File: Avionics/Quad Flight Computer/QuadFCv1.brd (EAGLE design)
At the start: 49.5 x 49.5 mm, 130 parts, among them J2 1050270001, Q1 DMP2035U, Q2 DMP2035U, Q3 DMP2035U, SW1 PTS635VL31-VERT, U1 TM4C123GH6PZ, U10 LTC4412, U11 AP7215-33YG-13, U2 74LVC4245APW, U3 ATMEGA32U2-MU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

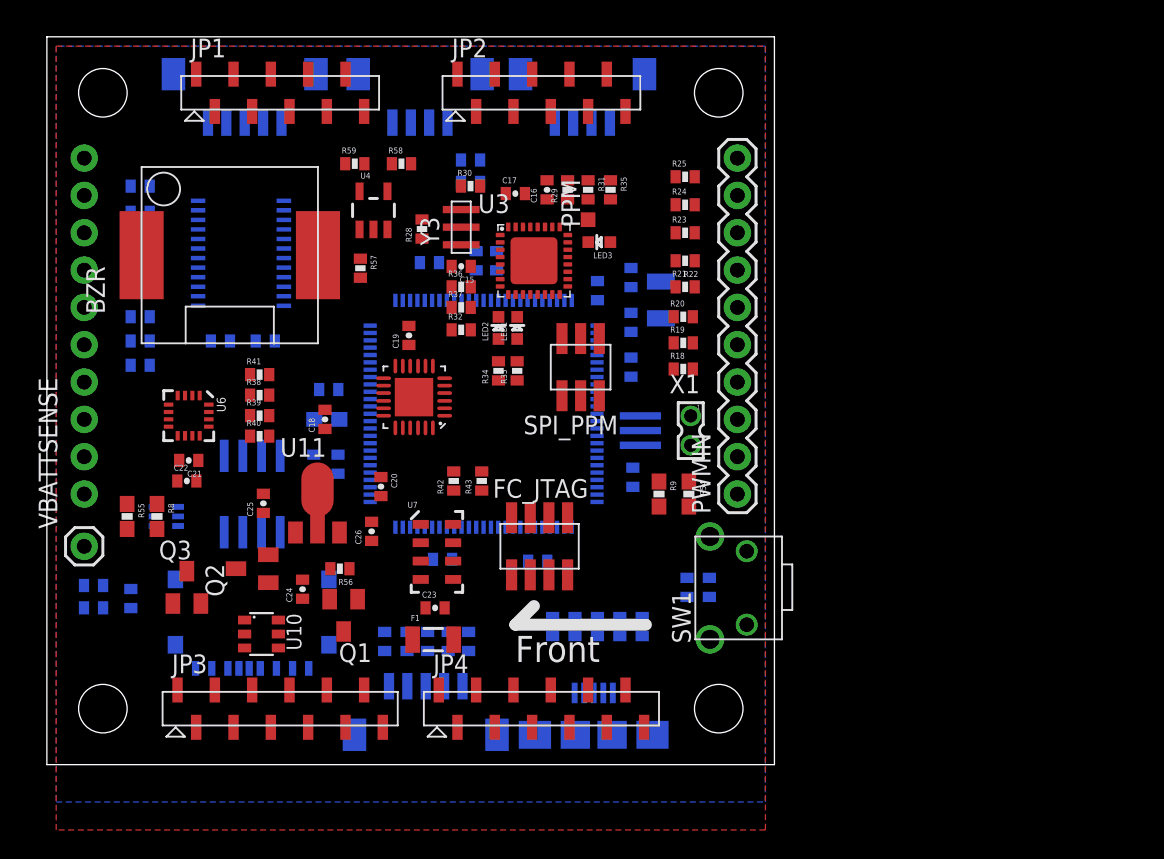
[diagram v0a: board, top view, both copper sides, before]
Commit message: Finished pinout for shield headers
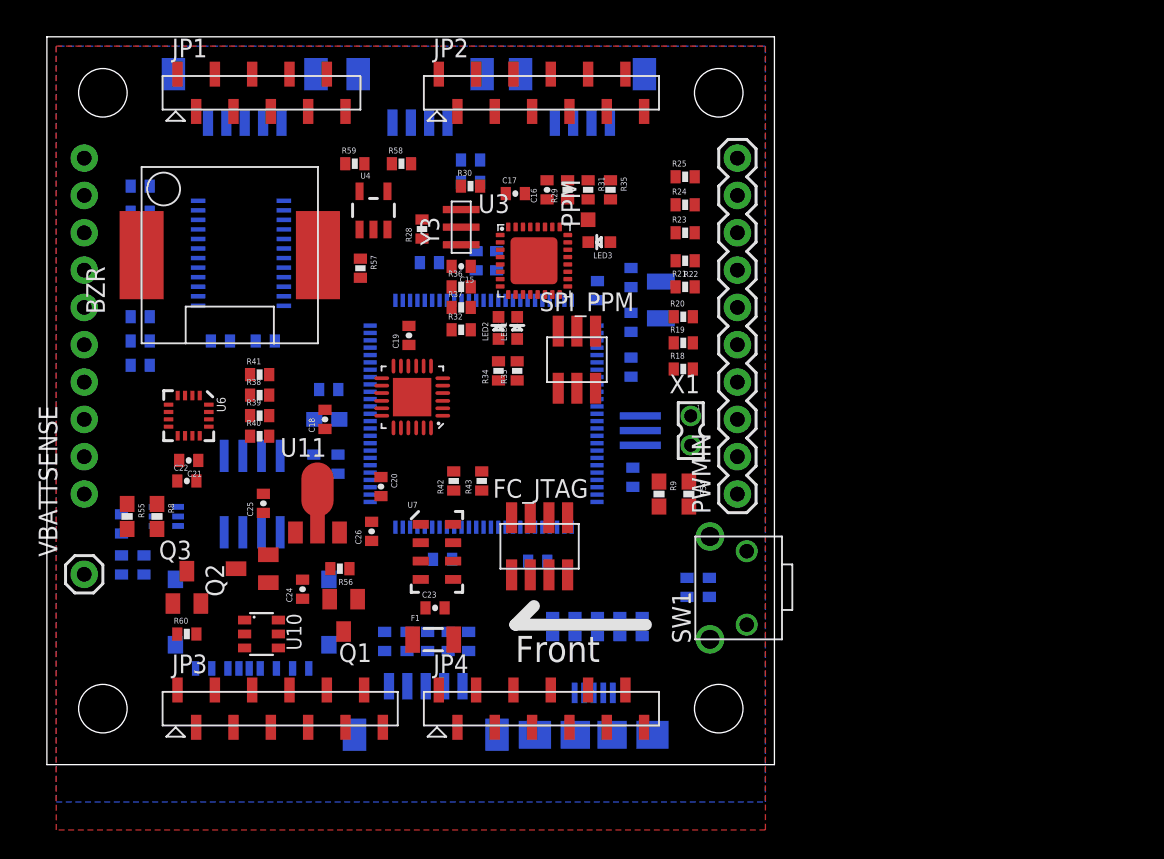
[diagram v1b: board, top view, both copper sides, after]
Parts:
- added R60: 100k, QuadFCv1:0402-RES
- JP2: value M101X10-SMT-0.05 -> M12; device QuadFCv1:1X10_SMT-0.05 -> QuadFCv1:1X12_SMT-0.05
- moved R46 5.12 mm to (5.08, 16.4)
- moved R45 4.50 mm to (6.60, 13.6), turned to 90 degrees
- moved R44 2.36 mm to (5.08, 13.6), turned to 270 degrees
- moved VBATTSENSE 1.90 mm to (2.54, 13.0)
- moved JP1 1.27 mm to (8.89, 45.7)
- moved JP2 1.27 mm to (26.7, 45.7)
- moved SPI_PPM 0.57 mm to (36.1, 27.6), turned to 0 degrees
- moved U5 0.13 mm to (24.9, 25.0)
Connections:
- net 3.3V: now also JP3.2
- net 5V: now also JP3.1
- net 5VBATT: now also R60.2
- net BUZZER_PWM: now also JP1.5
- net FC_IMU_MISO: now also JP2.2
- net FC_IMU_MOSI: now also JP2.3
- net FC_IMU_SCLK: now also JP2.1
- net FC_JTAG_TCK: now also JP4.5
- net FC_JTAG_TDI: now also JP4.7
- net FC_JTAG_TDO: now also JP4.8
- net FC_JTAG_TMS: now also JP4.6
- net FC_MEM_CLK: now also JP3.4
- net FC_MEM_MISO: now also JP3.5
- net FC_MEM_MOSI: now also JP3.3
- net FC_PB2: now also JP4.12
- net FC_PB3: now also JP4.11
- net FC_PB4: now also JP4.1
- net FC_PB5: now also JP4.2
- net FC_PD0: now also JP3.9
- net FC_PD1: now also JP3.8
- net FC_PD2: now also JP3.7
- net FC_PD3: now also JP3.6
- net FC_PD4: now also JP3.10
- net FC_PE4: now also JP3.12
- net FC_PE5: now also JP3.11
- net FC_PF0: now also JP2.4
- net FC_PF1: now also JP2.5
- net FC_PF2: now also JP2.6
- net FC_PF3: now also JP2.7
- net FC_PG2: now also JP2.10
- net FC_PG3: now also JP2.9
- net FC_PG4: now also JP4.10
- net FC_PG5: now also JP4.9
- net FC_PG6: now also JP4.4
- net FC_PG7: now also JP4.3
- net FC_RESET_L: now also JP2.8
- net FC_SENSE_SCL: now also JP2.11
- net FC_SENSE_SDA: now also JP2.12
- net GND: now also JP1.1, JP1.2
- net GPS_RX: now also JP1.6
- net GPS_TX: now also JP1.7
- net PPM_RX: now also JP1.8
- net PPM_TX: now also JP1.9
- net RADIO_RX: now also JP1.3
- net RADIO_TX: now also JP1.4
- net USB_EPEN: now also R60.1

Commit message: Some progress on routing
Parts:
- moved C10 8.41 mm to (20.3, 28.6)
- moved C14 2.34 mm to (18.7, 23.2)
- moved C7 1.90 mm to (39.8, 31.2)
- moved Y1 1.80 mm to (41.5, 29.8)
- moved L1 1.78 mm to (18.9, 21.7)
- moved C11 1.14 mm to (39.8, 29.0)
- moved C13 0.63 mm to (19.8, 19.8)
- moved C5 0.38 mm to (39.8, 26.7)
- turned R22 to 0 degrees
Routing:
- net 3.3V: track 0.00 -> 24.5 mm, vias 0 -> 6
- net 5VBATT: track 0.00 -> 16.7 mm
- net 5V: track 0.00 -> 15.8 mm
- net PWMIN1: track 0.00 -> 13.4 mm
- net FC_PWMOUT4: track 0.00 -> 13.4 mm
- net N$29: track 0.00 -> 13.2 mm
- net FC_PWMOUT3: track 0.00 -> 13.1 mm
- net FC_PWMOUT2: track 0.00 -> 12.9 mm
- net FC_PWMOUT1: track 0.00 -> 12.8 mm
- net PWMIN2: track 0.00 -> 12.0 mm
- net SD_CS_L: track 0.00 -> 11.3 mm
- net PWMIN8: track 0.00 -> 11.2 mm
- net PWMIN7: track 0.00 -> 10.4 mm
- net USB_POWER_CONN_L: track 0.00 -> 9.07 mm
- net PWMIN6: track 0.00 -> 8.81 mm
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
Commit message: Lots more routing done
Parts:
- removed R3, R5: 22-DNP, QuadFCv1:0402-RES
- removed R36: 1k, QuadFCv1:0402-RES
- removed R8, R9: DNP, QuadFCv1:0603-RES
- C12, C9: value 1uF -> 1.8uF
- moved C9 20.1 mm to (30.5, 14.2), turned to 270 degrees
- moved R43 4.67 mm to (25.3, 17.5)
- moved R42 4.09 mm to (24.0, 17.5)
- moved C20 3.19 mm to (24.7, 21.4), turned to 0 degrees
- moved R55 1.81 mm to (4.06, 15.7), turned to 0 degrees
- moved C3 1.71 mm to (41.5, 20.0)
- moved R54 1.51 mm to (42.4, 19.2), turned to 180 degrees
- moved R27 1.44 mm to (10.8, 29.8)
- moved R4 1.17 mm to (37.1, 9.14)
- moved R6 1.17 mm to (35.6, 9.14)
- moved C23 1.14 mm to (25.9, 11.7)
- moved R7 1.02 mm to (38.5, 9.40)
- moved R26 0.96 mm to (15.0, 29.8)
- moved U11 0.76 mm to (18.4, 17.0)
- moved C12 0.72 mm to (29.7, 33.8)
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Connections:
- removed net FC_USB_STATUS: R36.1, U1.39
- removed net N$28: R3.2, R7.2, U12.D-
- removed net PPM_USBDM: R3.1, U3.30
- removed net PPM_USBDP: R5.1, U3.29
- removed net PPM_USB_STATUS: R36.2, U3.5
- new net FC_PF4: JP2.8, U1.39
- new net N$49: R7.2, U12.D-
- net 5V: now also U3.31; no longer R8.2
- net 5VBATT: no longer R9.2
- net FC_PD4: now also JP3.12; no longer JP3.10
- net FC_PE4: now also JP3.10; no longer JP3.12
- net FC_RESET_L: now also JP1.10; no longer JP2.8
- net N$23: no longer R9.1
- net N$26: no longer R8.1
- net N$29: no longer R5.2
- net VUSB_F: no longer U3.31
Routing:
- net 3.3V: track 24.5 -> 71.4 mm, vias 6 -> 17
- net VUSB_F: track 4.92 -> 45.0 mm, vias 0 -> 3
- net USB_EPEN: track 2.20 -> 41.3 mm, vias 0 -> 1
- net 5V: track 15.8 -> 50.8 mm, vias 0 -> 4
- net RADIO_TX: track 0.00 -> 34.5 mm, vias 0 -> 1
- net FC_RESET_L: track 4.81 -> 38.0 mm, vias 0 -> 2
- net RADIO_RX: track 0.00 -> 32.5 mm, vias 0 -> 1
- net FC_SD_PRESENT: track 0.00 -> 31.4 mm, vias 0 -> 2
- net PPM_HWB: track 0.00 -> 28.8 mm
- net FC_JTAG_TDO: track 0.00 -> 27.6 mm, vias 0 -> 1
- net FC_JTAG_TDI: track 0.00 -> 22.7 mm, vias 0 -> 2
- net FC_JTAG_TMS: track 0.00 -> 21.4 mm, vias 0 -> 2
- net FC_PD3: track 0.00 -> 21.2 mm, vias 0 -> 1
- net VBATTSENSE: track 0.00 -> 21.1 mm
- net FC_MEM_MISO: track 0.00 -> 20.4 mm, vias 0 -> 1
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
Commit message: More routing
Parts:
- moved C18 2.97 mm to (21.3, 25.3), turned to 270 degrees
- moved R2 1.30 mm to (38.3, 33.3), turned to 180 degrees
- moved C5 0.92 mm to (40.5, 27.3), turned to 180 degrees
- moved C6 0.60 mm to (33.4, 33.8), turned to 180 degrees
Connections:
- net FC_IMU_MOSI: now also JP2.1; no longer JP2.3
- net FC_IMU_SCLK: now also JP2.3; no longer JP2.1
- net FC_PF0: now also JP2.5; no longer JP2.4
- net FC_PF1: now also JP2.6; no longer JP2.5
- net FC_PF2: now also JP2.7; no longer JP2.6
- net FC_PF3: now also JP2.8; no longer JP2.7
- net FC_PF4: now also JP2.4; no longer JP2.8
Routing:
- net FC_RESET_L: track 38.0 -> 103.7 mm
- net FC_SENSE_SCL: track 1.56 -> 45.0 mm, vias 0 -> 2
- net FC_SENSE_SDA: track 1.56 -> 35.8 mm, vias 0 -> 2
- net FC_PG3: track 0.00 -> 33.9 mm, vias 0 -> 1
- net GPS_TX: track 0.00 -> 30.5 mm, vias 0 -> 1
- net GPS_RX: track 0.00 -> 30.4 mm, vias 0 -> 1
- net FC_PG2: track 0.00 -> 27.9 mm, vias 0 -> 1
- net FC_IMU_MOSI: track 0.00 -> 21.6 mm, vias 0 -> 1
- net PPM_TX: track 0.00 -> 21.5 mm, vias 0 -> 1
- net FC_IMU_SCLK: track 0.00 -> 20.1 mm, vias 0 -> 1
- net FC_IMU_MISO: track 0.00 -> 18.3 mm, vias 0 -> 1
- net FC_PF3: track 0.00 -> 18.0 mm, vias 0 -> 1
- net FC_MEM_MOSI: track 2.45 -> 20.5 mm, vias 1 -> 3
- net PPM_RX: track 0.00 -> 17.5 mm, vias 0 -> 1
- net FC_PF2: track 0.00 -> 16.7 mm, vias 0 -> 1
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
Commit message: Only 4 wires left. Sooo close
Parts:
- removed LED1: RED, QuadFCv1:LED-0603
- removed LED2: ORANGE, QuadFCv1:LED-0603
- removed R33, R34: 1k, QuadFCv1:0402-RES
- moved R32 2.30 mm to (29.8, 31.2), turned to 90 degrees
- moved C25 1.02 mm to (14.8, 16.8)
- moved C15 0.80 mm to (27.5, 33.5), turned to 90 degrees
- moved R37 0.72 mm to (28.7, 31.6), turned to 90 degrees
- moved R53 0.41 mm to (28.8, 41.6)
- moved R52 0.25 mm to (28.8, 39.4)
- moved C19 0.19 mm to (24.8, 29.3)
- moved Y3 0.08 mm to (28.2, 36.7)
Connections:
- removed net N$30: LED1.A, R33.2
- removed net N$31: LED2.A, R34.2
- net 5V: no longer R33.1, R34.1
- net FC_IMU_INT: now also U1.22; no longer U1.58
- net FC_PPM_IN: now also U1.58; no longer U1.22
- net PPM_RX: no longer JP1.8
- net PPM_TX: no longer JP1.9
- net RXLED: no longer LED2.C
- net TXLED: no longer LED1.C
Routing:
- net 5V: track 59.0 -> 143.2 mm, vias 5 -> 9
- net FC_SENSE_SCL: track 45.0 -> 78.8 mm, vias 2 -> 5
- net FC_MEM_MISO: track 20.4 -> 52.4 mm, vias 1 -> 3
- net FC_SENSE_SDA: track 35.8 -> 66.5 mm, vias 2 -> 5
- net FC_MEM_MOSI: track 20.5 -> 51.1 mm, vias 3 -> 4
- net FC_MAG_DRDY_L: track 0.00 -> 28.9 mm, vias 0 -> 3
- net FC_MEM_CLK: track 15.5 -> 44.0 mm, vias 1 -> 3
- net FC_MEM_FSS: track 0.00 -> 27.8 mm, vias 0 -> 2
- net FC_PPM_IN: track 0.00 -> 22.0 mm, vias 0 -> 2
- net FC_IMU_SCLK: track 20.1 -> 35.6 mm, vias 1 -> 2
- net AUX_SDA: track 0.00 -> 15.4 mm, vias 0 -> 2
- net AUX_SCL: track 0.00 -> 14.1 mm, vias 0 -> 2
- net FC_IMU_MOSI: track 21.6 -> 35.6 mm, vias 1 -> 2
- net FC_IMU_CS_L: track 0.00 -> 12.8 mm, vias 0 -> 1
- net FC_IMU_MISO: track 18.3 -> 30.9 mm, vias 1 -> 2
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
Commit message: Finished routing and updated ariframe assembly
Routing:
- net FC_PWMOUT8: track 1.94 -> 37.7 mm, vias 1 -> 2
- net FC_PWMOUT6: track 1.66 -> 36.8 mm, vias 1 -> 2
- net FC_PWMOUT5: track 1.81 -> 36.2 mm, vias 1 -> 2
- net FC_PWMOUT7: track 1.78 -> 36.1 mm, vias 1 -> 2
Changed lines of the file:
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@@
 <setting verticaltext="up"/>
 </settings>
-<grid distance="1" unitdist="mil" unit="mil" style="lines" multiple="1" display="no" altdistance="0.025" altunitdist="inch" altunit="inch"/>
+<grid distance="1" unitdist="mil" unit="mm" style="lines" multiple="1" display="no" altdistance="0.025" altunitdist="inch" altunit="inch"/>
 <layers>
-<layer number="1" name="Top" color="4" fill="1" visible="no" active="yes"/>
-<layer number="2" name="VCC" color="1" fill="3" visible="no" active="yes"/>
+<layer number="1" name="Top" color="4" fill="1" visible="yes" active="yes"/>
+<layer number="2" name="VCC" color="1" fill="3" visible="yes" active="yes"/>
 <layer number="3" name="Route3" color="4" fill="3" visible="no" active="no"/>
 <layer number="14" name="Route14" color="1" fill="6" visible="no" active="no"/>
-<layer number="15" name="GND" color="4" fill="6" visible="yes" active="yes"/>
-<layer number="16" name="Bottom" color="1" fill="1" visible="no" active="yes"/>
+<layer number="15" name="GND" color="4" fill="6" visible="no" active="yes"/>
+<layer number="16" name="Bottom" color="1" fill="1" visible="yes" active="yes"/>
 <layer number="17" name="Pads" color="2" fill="1" visible="yes" active="yes"/>
 <layer number="18" name="Vias" color="2" fill="1" visible="yes" active="yes"/>
@@
 <wire x1="16.1258" y1="35.773" x2="14.8815" y2="35.773" width="0.1524" layer="16"/>
 <wire x1="14.8815" y1="35.773" x2="14.478" y2="35.3695" width="0.1524" layer="16"/>
-<wire x1="16.1258" y1="35.773" x2="34.218" y2="16.156" width="0" layer="19" extent="16-16"/>
+<via x="31.0388" y="22.1742" extent="1-16" drill="0.4064"/>
+<wire x1="34.218" y1="16.156" x2="34.218" y2="18.233" width="0.1524" layer="16"/>
+<wire x1="34.218" y1="18.233" x2="31.4452" y2="21.0058" width="0.1524" layer="16"/>
+<wire x1="31.4452" y1="21.0058" x2="31.4452" y2="21.7678" width="0.1524" layer="16"/>
+<wire x1="31.4452" y1="21.7678" x2="31.0388" y2="22.1742" width="0.1524" layer="16"/>
+<wire x1="31.0388" y1="22.1742" x2="31.0388" y2="23.2156" width="0.1524" layer="2"/>
+<wire x1="31.0388" y1="23.2156" x2="30.5562" y2="23.6982" width="0.1524" layer="2"/>
+<wire x1="30.5562" y1="23.6982" x2="30.0736" y2="23.6982" width="0.1524" layer="2"/>
+<wire x1="30.0736" y1="23.6982" x2="29.3116" y2="24.4602" width="0.1524" layer="2"/>
+<wire x1="29.3116" y1="24.4602" x2="29.3116" y2="27.2542" width="0.1524" layer="2"/>
+<wire x1="29.3116" y1="27.2542" x2="27.8384" y2="28.7274" width="0.1524" layer="2"/>
+<wire x1="27.8384" y1="28.7274" x2="25.0952" y2="28.7274" width="0.1524" layer="2"/>
+<wire x1="25.0952" y1="28.7274" x2="23.749" y2="27.3812" width="0.1524" layer="2"/>
+<wire x1="23.749" y1="27.3812" x2="22.8854" y2="27.3812" width="0.1524" layer="2"/>
+<wire x1="22.8854" y1="27.3812" x2="22.2504" y2="28.0162" width="0.1524" layer="2"/>
+<wire x1="22.2504" y1="28.0162" x2="21.3868" y2="28.0162" width="0.1524" layer="2"/>
+<wire x1="21.3868" y1="28.0162" x2="19.431" y2="29.972" width="0.1524" layer="2"/>
+<wire x1="19.431" y1="29.972" x2="19.431" y2="32.7914" width="0.1524" layer="2"/>
+<wire x1="19.431" y1="32.7914" x2="16.9418" y2="35.2806" width="0.1524" layer="2"/>
+<wire x1="16.9418" y1="35.2806" x2="16.8656" y2="35.3568" width="0.1524" layer="2"/>
+<wire x1="16.8656" y1="35.3568" x2="14.4907" y2="35.3568" width="0.1524" layer="2"/>
+<wire x1="14.4907" y1="35.3568" x2="14.478" y2="35.3695" width="0.1524" layer="2"/>
 </signal>
 <signal name="FC_PWMOUT6">
@@
 <wire x1="16.1258" y1="36.423" x2="14.5155" y2="36.423" width="0.1524" layer="16"/>
 <wire x1="14.5155" y1="36.423" x2="14.478" y2="36.3855" width="0.1524" layer="16"/>
-<wire x1="16.1258" y1="36.423" x2="34.718" y2="16.156" width="0" layer="19" extent="16-16"/>
+<via x="32.0294" y="22.1742" extent="1-16" drill="0.4064"/>
+<wire x1="34.718" y1="16.156" x2="34.718" y2="18.241" width="0.1524" layer="16"/>
+<wire x1="34.718" y1="18.241" x2="32.0294" y2="20.9296" width="0.1524" layer="16"/>
+<wire x1="32.0294" y1="20.9296" x2="32.0294" y2="22.1742" width="0.1524" layer="16"/>
+<wire x1="32.0294" y1="22.1742" x2="32.0294" y2="22.6822" width="0.1524" layer="2"/>
+<wire x1="32.0294" y1="22.6822" x2="30.7086" y2="24.003" width="0.1524" layer="2"/>
+<wire x1="30.7086" y1="24.003" x2="30.226" y2="24.003" width="0.1524" layer="2"/>
+<wire x1="30.226" y1="24.003" x2="29.6418" y2="24.5872" width="0.1524" layer="2"/>
+<wire x1="29.6418" y1="24.5872" x2="29.6418" y2="27.3812" width="0.1524" layer="2"/>
+<wire x1="29.6418" y1="27.3812" x2="27.9908" y2="29.0322" width="0.1524" layer="2"/>
+<wire x1="27.9908" y1="29.0322" x2="24.9682" y2="29.0322" width="0.1524" layer="2"/>
+<wire x1="24.9682" y1="29.0322" x2="23.622" y2="27.686" width="0.1524" layer="2"/>
+<wire x1="23.622" y1="27.686" x2="23.0378" y2="27.686" width="0.1524" layer="2"/>
+<wire x1="23.0378" y1="27.686" x2="22.5806" y2="28.1432" width="0.1524" layer="2"/>
+<wire x1="22.5806" y1="28.1432" x2="22.5806" y2="30.7086" width="0.1524" layer="2"/>
+<wire x1="22.5806" y1="30.7086" x2="20.7772" y2="32.512" width="0.1524" layer="2"/>
+<wire x1="20.7772" y1="32.512" x2="17.018" y2="36.2712" width="0.1524" layer="2"/>
+<wire x1="17.018" y1="36.2712" x2="16.8656" y2="36.4236" width="0.1524" layer="2"/>
+<wire x1="16.8656" y1="36.4236" x2="14.5161" y2="36.4236" width="0.1524" layer="2"/>
+<wire x1="14.5161" y1="36.4236" x2="14.478" y2="36.3855" width="0.1524" layer="2"/>
 </signal>
 <signal name="FC_PWMOUT7">
@@
 <wire x1="16.1258" y1="37.073" x2="14.8065" y2="37.073" width="0.1524" layer="16"/>
 <wire x1="14.8065" y1="37.073" x2="14.478" y2="37.4015" width="0.1524" layer="16"/>
-<wire x1="16.1258" y1="37.073" x2="35.218" y2="16.156" width="0" layer="19" extent="16-16"/>
+<via x="33.0454" y="22.1742" extent="1-16" drill="0.4064"/>
+<wire x1="35.218" y1="16.156" x2="35.218" y2="18.3252" width="0.1524" layer="16"/>
+<wire x1="35.218" y1="18.3252" x2="33.02" y2="20.5232" width="0.1524" layer="16"/>
+<wire x1="33.02" y1="20.5232" x2="33.02" y2="22.1488" width="0.1524" layer="16"/>
+<wire x1="33.02" y1="22.1488" x2="33.0454" y2="22.1742" width="0.1524" layer="16"/>
+<wire x1="33.0454" y1="22.1742" x2="33.0454" y2="22.1996" width="0.1524" layer="2"/>
+<wire x1="33.0454" y1="22.1996" x2="32.1818" y2="23.0632" width="0.1524" layer="2"/>
+<wire x1="32.1818" y1="23.0632" x2="32.1818" y2="26.0096" width="0.1524" layer="2"/>
+<wire x1="32.1818" y1="26.0096" x2="30.607" y2="27.5844" width="0.1524" layer="2"/>
+<wire x1="30.607" y1="27.5844" x2="30.5054" y2="27.5844" width="0.1524" layer="2"/>
+<wire x1="30.5054" y1="27.5844" x2="29.6164" y2="28.4734" width="0.1524" layer="2"/>
+<wire x1="29.6164" y1="28.4734" x2="29.6164" y2="29.8196" width="0.1524" layer="2"/>
+<wire x1="29.6164" y1="29.8196" x2="28.0416" y2="31.3944" width="0.1524" layer="2"/>
+<wire x1="28.0416" y1="31.3944" x2="24.2316" y2="31.3944" width="0.1524" layer="2"/>
+<wire x1="24.2316" y1="31.3944" x2="22.9362" y2="32.6898" width="0.1524" layer="2"/>
+<wire x1="22.9362" y1="32.6898" x2="21.0566" y2="32.6898" width="0.1524" layer="2"/>
+<wire x1="21.0566" y1="32.6898" x2="16.6878" y2="37.0586" width="0.1524" layer="2"/>
+<wire x1="16.6878" y1="37.0586" x2="14.8209" y2="37.0586" width="0.1524" layer="2"/>
+<wire x1="14.8209" y1="37.0586" x2="14.478" y2="37.4015" width="0.1524" layer="2"/>
 </signal>
 <signal name="FC_PWMOUT8">
@@
 <wire x1="16.1258" y1="37.723" x2="15.1725" y2="37.723" width="0.1524" layer="16"/>
 <wire x1="15.1725" y1="37.723" x2="14.478" y2="38.4175" width="0.1524" layer="16"/>
-<wire x1="16.1258" y1="37.723" x2="35.718" y2="16.156" width="0" layer="19" extent="16-16"/>
+<via x="33.0454" y="23.1902" extent="1-16" drill="0.4064"/>
+<wire x1="35.718" y1="16.156" x2="35.718" y2="18.3078" width="0.1524" layer="16"/>
+<wire x1="35.718" y1="18.3078" x2="33.7058" y2="20.32" width="0.1524" layer="16"/>
+<wire x1="33.7058" y1="20.32" x2="33.7058" y2="22.5298" width="0.1524" layer="16"/>
+<wire x1="33.7058" y1="22.5298" x2="33.0454" y2="23.1902" width="0.1524" layer="16"/>
+<wire x1="33.0454" y1="23.1902" x2="32.9184" y2="23.1902" width="0.1524" layer="2"/>
+<wire x1="32.9184" y1="23.1902" x2="32.4866" y2="23.622" width="0.1524" layer="2"/>
+<wire x1="32.4866" y1="23.622" x2="32.4866" y2="26.162" width="0.1524" layer="2"/>
+<wire x1="32.4866" y1="26.162" x2="30.3784" y2="28.2702" width="0.1524" layer="2"/>
+<wire x1="30.3784" y1="28.2702" x2="29.9212" y2="28.7274" width="0.1524" layer="2"/>
+<wire x1="29.9212" y1="28.7274" x2="29.9212" y2="29.972" width="0.1524" layer="2"/>
+<wire x1="29.9212" y1="29.972" x2="28.1686" y2="31.7246" width="0.1524" layer="2"/>
+<wire x1="28.1686" y1="31.7246" x2="25.1968" y2="31.7246" width="0.1524" layer="2"/>
+<wire x1="25.1968" y1="31.7246" x2="24.9174" y2="32.004" width="0.1524" layer="2"/>
+<wire x1="24.9174" y1="32.004" x2="24.9174" y2="32.9438" width="0.1524" layer="2"/>
+<wire x1="24.9174" y1="32.9438" x2="24.4856" y2="33.3756" width="0.1524" layer="2"/>
+<wire x1="24.4856" y1="33.3756" x2="24.257" y2="33.3756" width="0.1524" layer="2"/>
+<wire x1="24.257" y1="33.3756" x2="23.4188" y2="34.2138" width="0.1524" layer="2"/>
+<wire x1="23.4188" y1="34.2138" x2="20.0152" y2="34.2138" width="0.1524" layer="2"/>
+<wire x1="20.0152" y1="34.2138" x2="16.7386" y2="37.4904" width="0.1524" layer="2"/>
+<wire x1="16.7386" y1="37.4904" x2="15.4051" y2="37.4904" width="0.1524" layer="2"/>
+<wire x1="15.4051" y1="37.4904" x2="14.478" y2="38.4175" width="0.1524" layer="2"/>
 </signal>
 <signal name="N$17">
